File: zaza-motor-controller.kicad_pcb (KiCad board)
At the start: 2 copper layers, 53 x 60 mm, 74 parts, among them J1 VIN, J2 VIN, J3 CONN_02X05, J4 CONN_02X01, J5 GS3, Q1 BC337, Q10 BC327, Q11 BC337, Q12 BC337, Q2 BC337, Q3 BC327, Q4 BC337, Q5 IXTA220, Q6 IXTA220, Q7 IXTA220, Q8 IXTA220, Q9 BC337, U1 74HC00, U2 74HC00, U3 LM358, U4 LM555N

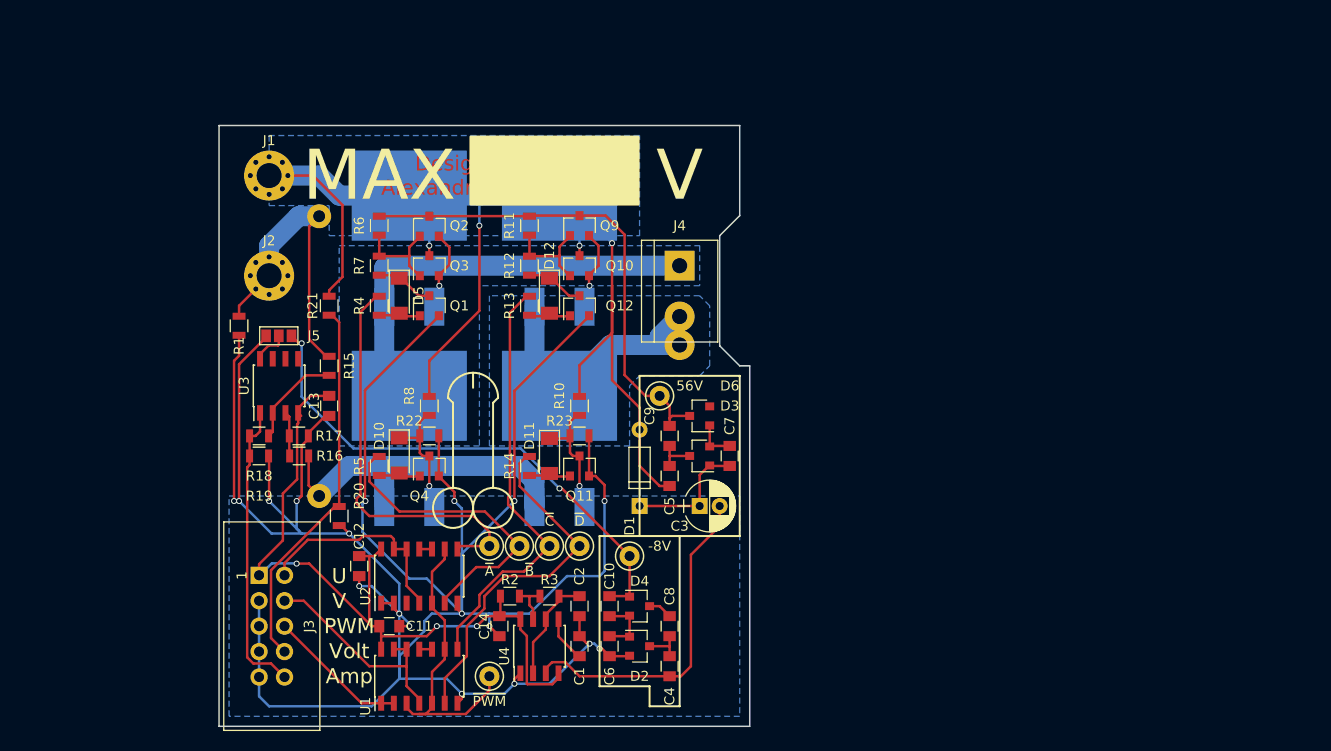
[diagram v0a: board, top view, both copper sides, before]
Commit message: Add layout for Revision 1
Now made to fit in an off-the-shelf plastic box.
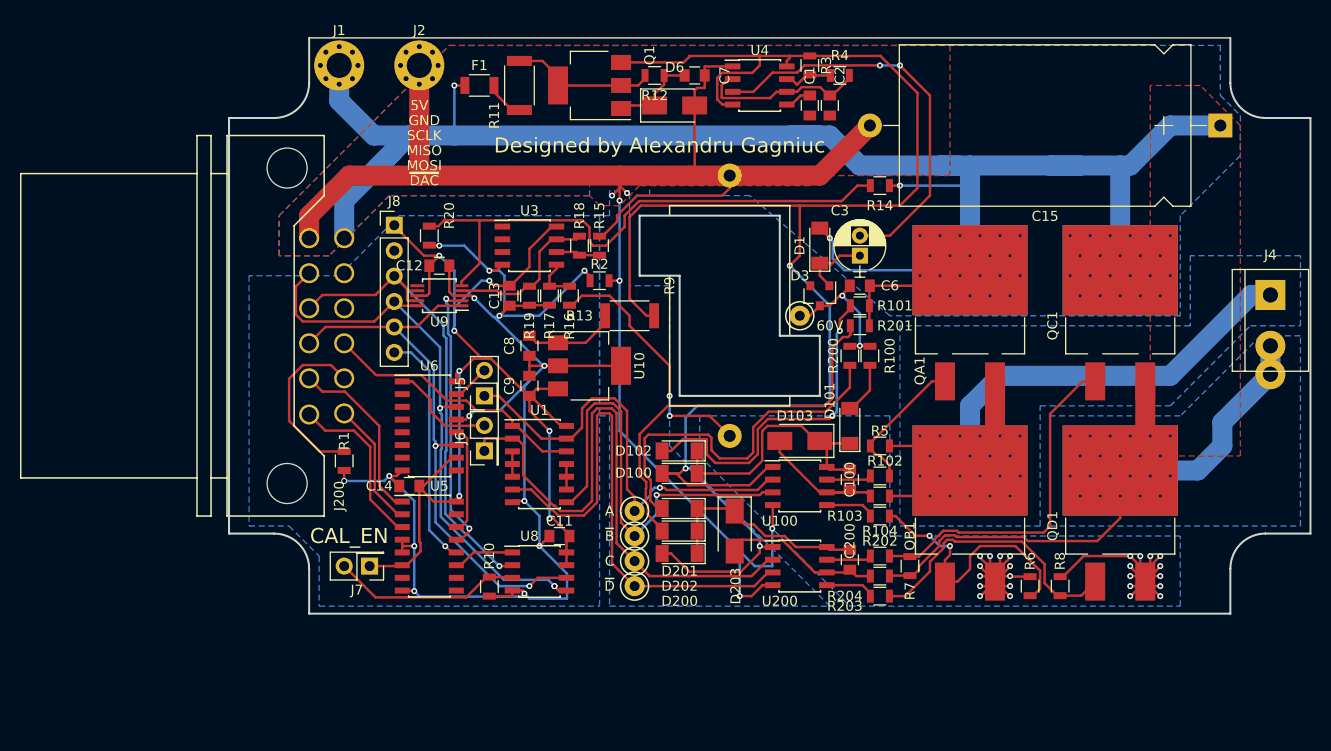
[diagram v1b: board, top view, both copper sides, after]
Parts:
- removed C10, C4, C5: 1uF, Capacitors_SMD:C_0805
- removed D10, D11, D12, D5: BAT5H17, Diodes_SMD:D_MiniMELF_Standard
- removed D2, D4: BAR43, TO_SOT_Packages_SMD:SOT-23
- removed J3: CONN_02X05, Connectors:IDC_Header_Straight_10pins
- removed Q10, Q3: BC327, TO_SOT_Packages_SMD:SOT-23
- removed Q11, Q12, Q2, Q4, Q9: BC337, TO_SOT_Packages_SMD:SOT-23
- removed Q5, Q6, Q7, Q8: IXTA220, TO_SOT_Packages_SMD:SOT-404
- removed R21: 180k, Resistors_SMD:R_0805
- removed R22, R23: 3.3k, Resistors_SMD:R_0805
- removed TP2: -8V, Measurement_Points:Test_Point_Keystone_5000-5004_Miniature
- removed TP3: 56V, Measurement_Points:Test_Point_Keystone_5000-5004_Miniature
- removed U2: 74HC00, Housings_SOIC:SOIC-14_3.9x8.7mm_Pitch1.27mm
- added C100: 220n, Capacitors_SMD:C_0805, F.Cu at (163.0, 95.4)
- added C15: 100u 100V, Capacitors_THT:CP_Axial_L29.0mm_D16.0mm_P35.00mm_Horizontal, F.Cu at (200.0, 60.0)
- added C200: 220n, Capacitors_SMD:C_0805, F.Cu at (163.0, 103.4)
- added D100: 1N..., Diodes_SMD:D_MiniMELF_Standard, F.Cu at (146.0, 94.8)
- added D101: 1N..., Diodes_SMD:D_MiniMELF_Standard, F.Cu at (163.0, 90.0)
- added D102: 1N..., Diodes_SMD:D_MiniMELF_Standard, F.Cu at (146.0, 92.5)
- added D103: 15.6V, Diodes_SMD:D_SMA_Standard, F.Cu at (158.0, 91.5)
- added D200: 1N..., Diodes_SMD:D_MiniMELF_Standard, F.Cu at (146.0, 102.8)
- added D201: 1N..., Diodes_SMD:D_MiniMELF_Standard, F.Cu at (146.0, 98.2)
- added D202: 1N..., Diodes_SMD:D_MiniMELF_Standard, F.Cu at (146.0, 100.5)
- added D203: 15.6V, Diodes_SMD:D_SMA_Standard, F.Cu at (151.5, 100.5)
- added F1: 100mA, Resistors_SMD:R_1206, F.Cu at (126.0, 56.0)
- added J200: MX120G, molex-120g:Molex_MX120G_02x06_3.5mm_36783-1201, F.Cu at (112.5, 80.0)
- added J6: V, Pin_Headers:Pin_Header_Straight_2x01_Pitch2.54mm, F.Cu at (126.5, 92.5)
- added J7: CAL_EN, Pin_Headers:Pin_Header_Straight_2x01_Pitch2.54mm, F.Cu at (115.0, 104.0)
- added J8: CONN_01X06, Pin_Headers:Pin_Header_Straight_1x06_Pitch2.54mm, F.Cu at (117.5, 70.0)
- added QA1: DMN10, TO-SMD:SOT-404-thermal-vias, F.Cu at (175.0, 80.0)
- added QB1: DMN10, TO-SMD:SOT-404-thermal-vias, F.Cu at (175.0, 100.0)
- added QC1: DMN10, TO-SMD:SOT-404-thermal-vias, F.Cu at (190.0, 80.0)
- added QD1: DMN10, TO-SMD:SOT-404-thermal-vias, F.Cu at (190.0, 100.0)
- added R100: 10k, Resistors_SMD:R_0805, F.Cu at (165.0, 83.0)
- added R101: 10k, Resistors_SMD:R_0805, F.Cu at (164.0, 78.0)
- added R102: 1k, Resistors_SMD:R_0805, F.Cu at (166.0, 95.0)
- added R103: 0R, Resistors_SMD:R_0805, F.Cu at (166.0, 97.0)
- added R104: 1k, Resistors_SMD:R_0805, F.Cu at (166.0, 99.0)
- added R200: 10k, Resistors_SMD:R_0805, F.Cu at (163.0, 83.0)
- added R201: 10k, Resistors_SMD:R_0805, F.Cu at (164.0, 80.0)
- added R202: 1k, Resistors_SMD:R_0805, F.Cu at (166.0, 103.0)
- added R203: 0R, Resistors_SMD:R_0805, F.Cu at (166.0, 105.0)
- added R204: 1k, Resistors_SMD:R_0805, F.Cu at (166.0, 107.0)
- added U10: LM7805CT, TO_SOT_Packages_SMD:SOT-223-3Lead_TabPin2, F.Cu at (137.0, 84.0)
- added U100: IRS2003, Housings_SOIC:SOIC-8_3.9x4.9mm_Pitch1.27mm, F.Cu at (158.0, 96.0)
- added U200: IRS2003, Housings_SOIC:SOIC-8_3.9x4.9mm_Pitch1.27mm, F.Cu at (158.0, 104.0)
- added U5: 74xx138, Housings_SOIC:SOIC-16_3.9x9.9mm_Pitch1.27mm, F.Cu at (121.0, 102.0)
- added U6: 74xx595, Housings_SOIC:SOIC-16_3.9x9.9mm_Pitch1.27mm, F.Cu at (121.0, 90.0)
- added U8: AT25XX, Housings_SOIC:SOIC-8_3.9x4.9mm_Pitch1.27mm, F.Cu at (132.0, 104.5)
- added U9: ADS1018, Housings_SSOP:MSOP-10_3x3mm_Pitch0.5mm, F.Cu at (122.0, 77.0)
- C1: value 100p -> 1n
- C2: value 1nF -> 100p
- D1: footprint Diodes_THT:D_DO-35_SOD27_P7.62mm_Horizontal -> Diodes_SMD:D_MiniMELF_Standard
- D6: value BAR43 -> 15.6V; footprint TO_SOT_Packages_SMD:SOT-23 -> Diodes_SMD:D_SMA_Standard
- J5: value GS3 -> U; footprint Connectors:GS3 -> Pin_Headers:Pin_Header_Straight_2x01_Pitch2.54mm
- Q1: value BC337 -> NZT605; footprint TO_SOT_Packages_SMD:SOT-23 -> TO_SOT_Packages_SMD:SOT-223-3Lead_TabPin2
- R11, R13: value 10k -> 50R; footprint Resistors_SMD:R_0805 -> Resistors_SMD:R_2010
- R12: value 50k -> 10k
- R14: value 10k -> 180k
- R2: value 10k -> 0R
- R3: value 47k -> 10k
- R4: value 10k -> 47k
- R5, R6, R8: value 10k -> 1M
- R7: value 50k -> 1M
- R9: moved to F.Cu
- TP1: value ~PWM -> 60V
- TP4: value ~A -> A
- TP7: value ~C -> C
- moved R6 74.3 mm to (181.0, 106.0), turned to 90 degrees
- moved R8 65.5 mm to (184.0, 106.0), turned to 90 degrees
- moved R7 60.9 mm to (169.0, 104.0)
- moved U4 60.2 mm to (154.0, 56.0), turned to 0 degrees
- moved J4 59.1 mm to (205.0, 76.9)
- moved R3 59.0 mm to (159.0, 54.0), turned to 270 degrees
- moved C1 58.7 mm to (159.0, 58.0), turned to 270 degrees
- moved C2 55.9 mm to (161.0, 58.0)
- moved R4 51.4 mm to (162.0, 55.0), turned to 0 degrees
- moved R5 50.0 mm to (166.0, 92.0), turned to 0 degrees
- moved TP1 47.5 mm to (158.0, 79.0)
- moved R9 45.2 mm to (151.0, 78.0)
- moved R14 44.8 mm to (166.0, 66.0), turned to 0 degrees
- moved C6 43.8 mm to (164.0, 76.0), turned to 0 degrees
- moved C7 38.2 mm to (147.5, 55.0), turned to 0 degrees
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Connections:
- C1 pad 2: GND -> GNDPWR
- C2 pad 2: GND -> GNDPWR
- C6 pad 1: Net-(C10-Pad2) -> HT
- C6 pad 2: GND -> +48V
- C7 pad 2: Net-(C3-Pad1) -> GNDPWR
- C8 pad 2: Net-(C4-Pad1) -> GND
- C9 pad 1: HT -> +5V
- C9 pad 2: Net-(C5-Pad1) -> GND
- D3 pad 2: Net-(C7-Pad1) -> (no net)
- D3 pad 3: Net-(C5-Pad1) -> HT
- D6 pad 2: Net-(D6-Pad2) -> GNDPWR
- J5 pad 1: GND -> /A
- Q1 pad 1: Net-(D5-Pad2) -> Net-(C7-Pad1)
- Q1 pad 2: GND -> Net-(Q1-Pad2)
- Q1 pad 3: Net-(D5-Pad1) -> +15V
- R1 pad 1: GND -> GNDREF
- R1 pad 2: GNDPWR -> GND
- R10 pad 1: +48V -> Net-(J7-Pad2)
- R10 pad 2: Net-(D11-Pad1) -> GND
- R11 pad 1: HT -> Net-(F1-Pad1)
- R11 pad 2: Net-(Q10-Pad1) -> Net-(Q1-Pad2)
- R12 pad 1: Net-(Q10-Pad1) -> Net-(C7-Pad1)
- R12 pad 2: Net-(D12-Pad1) -> Net-(Q1-Pad2)
- R13 pad 1: /~C -> +15V
- R13 pad 2: Net-(D12-Pad2) -> Net-(C8-Pad1)
- R14 pad 1: /~D -> /V_SENSE
- R14 pad 2: Net-(D11-Pad2) -> +48V
- R16 pad 1: Net-(Q6-Pad3) -> Net-(QB1-Pad3)
- R2 pad 1: +5V -> GND
- R2 pad 2: Net-(R2-Pad2) -> GNDPWR
- R3 pad 1: Net-(R2-Pad2) -> +15V
- R3 pad 2: Net-(C2-Pad1) -> Net-(R3-Pad2)
- R4 pad 1: /~A -> Net-(R3-Pad2)
- R4 pad 2: Net-(D5-Pad2) -> Net-(C2-Pad1)
- R5 pad 1: /~B -> Net-(QA1-Pad1)
- R5 pad 2: Net-(D10-Pad2) -> /M+
- R6 pad 1: HT -> Net-(QB1-Pad1)
- R6 pad 2: Net-(Q2-Pad1) -> Net-(QB1-Pad3)
- R7 pad 1: Net-(Q2-Pad1) -> Net-(QC1-Pad1)
- R7 pad 2: Net-(D5-Pad1) -> /M-
- R8 pad 1: +48V -> Net-(QD1-Pad1)
- R8 pad 2: Net-(D10-Pad1) -> Net-(QB1-Pad3)
- R9 pad 1: Net-(Q6-Pad3) -> Net-(QB1-Pad3)
- TP1 pad 1: /~PWM -> HT
- TP4 pad 1: /~A -> /A
- TP7 pad 1: /~C -> /C
- U1 pad 1: /EN -> /PWM
- U1 pad 10: /~V -> Net-(U1-Pad10)
- U1 pad 11: /~V -> Net-(U1-Pad10)
- U1 pad 12: /V -> /PWM
- U1 pad 13: /V -> /A
- U1 pad 2: /EN -> /C
- U1 pad 3: /~PWM -> Net-(U1-Pad3)
- U1 pad 4: /V -> Net-(U1-Pad3)
- U1 pad 5: /~PWM -> Net-(U1-Pad3)
- U1 pad 8: /~C -> /~B
- U1 pad 9: /~PWM -> Net-(U1-Pad10)
- U3 pad 1: /I_SENSE -> (no net)
- U3 pad 2: Net-(R15-Pad2) -> (no net)
- U3 pad 3: Net-(R16-Pad2) -> (no net)
- U3 pad 4: +5V -> GND
- U3 pad 5: (no net) -> Net-(R16-Pad2)
- U3 pad 6: (no net) -> Net-(R15-Pad2)
- U3 pad 7: (no net) -> /I_SENSE
- U3 pad 8: Net-(J5-Pad2) -> +5V
- U4 pad 1: GND -> GNDPWR
- U4 pad 4: +5V -> +15V
- U4 pad 7: Net-(R2-Pad2) -> Net-(R3-Pad2)
- U4 pad 8: +5V -> +15V
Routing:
- net +15V: track 0.00 -> 173.9 mm, vias 0 -> 3
- net GND: track 293.1 -> 142.0 mm, vias 18 -> 14
- net GNDPWR: track 29.9 -> 172.1 mm, vias 0 -> 6
- net Net-(QB1-Pad3): track 0.00 -> 90.0 mm, vias 0 -> 26
- net /C: track 0.00 -> 59.7 mm
- net /MOSI: track 0.00 -> 59.1 mm, vias 0 -> 3
- net +48V: track 137.1 -> 193.8 mm, vias 4 -> 3
- net /SCLK: track 0.00 -> 56.4 mm, vias 0 -> 2
- net VEE: track 52.1 -> 0.00 mm, vias 2 -> 0
- net /MISO: track 0.00 -> 48.6 mm, vias 0 -> 1
- net /A: track 0.00 -> 45.8 mm, vias 0 -> 1
- net /~C: track 43.1 -> 0.00 mm
- net /~A: track 41.0 -> 0.00 mm
- net Net-(D202-Pad2): track 0.00 -> 39.7 mm
- net Net-(D201-Pad2): track 0.00 -> 37.0 mm
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- added copper zone on B.Cu, net GNDPWR
- added copper zone on F.Cu, net GNDPWR
- added copper zone on B.Cu, net Net-(QB1-Pad3)
- added copper zone on F.Cu, net Net-(QB1-Pad3)
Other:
- board size 53 x 60 mm -> 108 x 57.5 mm
- net class Default: via_drill 0.4 -> 0.3
- net class PWR: via_drill 0.4 -> 0.3
- net class PWR-small: via_drill 0.4 -> 0.3
- board text added: "5V"
- board text added: "Approximate dimensions of Hammond 1591XXB box"
- board text added: "GND"
- board text added: "MISO"
- board text added: "MOSI"
- board text added: "SCLK"
- board text added: "~DAC"
- board text removed: "Amp"
- board text removed: "MAX"
- board text removed: "PWM"
- board text removed: "U"
- board text removed: "V"
- board text removed: "Volt"

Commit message: Organize F. Fab layer to emphasize compnent values
The F. Fab layer is useful for manual assembly. In this case, it's
very useful to emphasize the component values.
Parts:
- U10: value LM7805CT -> LM7805
- U4: value LM555N -> LM555
- U5: value 74xx138 -> 74HC138
- U6: value 74xx595 -> 74HC595
- U8: value AT25XX -> AT25
